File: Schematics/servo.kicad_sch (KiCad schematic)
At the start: 0 parts

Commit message: Power + Servo
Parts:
- added M?: Motor_Servo, symbol Motor:Motor_Servo
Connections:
- new net +5V: M?.2 (+)
- new net Earth: M?.3 (-)
- new net ServoPWM: M?.1 (PWM)
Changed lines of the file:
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@@
 (kicad_sch (version 20211123) (generator eeschema)
   (paper "A4")
+  (wire (pts (xy 137.16 102.87) (xy 137.16 101.6))
+    (stroke (width 0) (type default) (color 0 0 0 0))
+  )
+  (wire (pts (xy 143.51 100.33) (xy 140.97 100.33))
+    (stroke (width 0) (type default) (color 0 0 0 0))
+  )
+  (wire (pts (xy 140.97 100.33) (xy 140.97 95.25))
+    (stroke (width 0) (type default) (color 0 0 0 0))
+  )
+  (wire (pts (xy 143.51 105.41) (xy 137.16 105.41))
+    (stroke (width 0) (type default) (color 0 0 0 0))
+  )
+  (wire (pts (xy 143.51 102.87) (xy 137.16 102.87))
+    (stroke (width 0) (type default) (color 0 0 0 0))
+  )
+  (wire (pts (xy 137.16 105.41) (xy 137.16 106.68))
+    (stroke (width 0) (type default) (color 0 0 0 0))
+  )
+  (wire (pts (xy 140.97 95.25) (xy 146.05 95.25))
+    (stroke (width 0) (type default) (color 0 0 0 0))
+  )
+  (global_label "ServoPWM" (shape input) (at 146.05 95.25 0) (fields_autoplaced)
+    (effects (font (size 1.27 1.27)) (justify left))
+    (property "Intersheet References" "${INTERSHEET_REFS}" (id 0) (at 157.8369 95.1706 0)
+      (effects (font (size 1.27 1.27)) (justify left) hide)
+    )
+  )
+  (symbol (lib_id "power:+5V") (at 137.16 101.6 0) (unit 1)
+    (in_bom yes) (on_board yes) (fields_autoplaced)
+    (property "Reference" "#PWR?" (id 0) (at 137.16 105.41 0)
+      (effects (font (size 1.27 1.27)) hide)
+    )
+    (property "Value" "+5V" (id 1) (at 137.16 96.52 0))
+    (property "Footprint" "" (id 2) (at 137.16 101.6 0)
+      (effects (font (size 1.27 1.27)) hide)
+    )
+    (property "Datasheet" "" (id 3) (at 137.16 101.6 0)
+      (effects (font (size 1.27 1.27)) hide)
+    )
+    (pin "1")
+  )
+  (symbol (lib_id "power:Earth") (at 137.16 106.68 0) (unit 1)
+    (in_bom yes) (on_board yes) (fields_autoplaced)
+    (property "Reference" "#PWR?" (id 0) (at 137.16 113.03 0)
+      (effects (font (size 1.27 1.27)) hide)
+    )
+    (property "Value" "Earth" (id 1) (at 137.16 110.49 0)
+      (effects (font (size 1.27 1.27)) hide)
+    )
+    (property "Footprint" "" (id 2) (at 137.16 106.68 0)
+      (effects (font (size 1.27 1.27)) hide)
+    )
+    (property "Datasheet" "~" (id 3) (at 137.16 106.68 0)
+      (effects (font (size 1.27 1.27)) hide)
+    )
+    (pin "1")
+  )
+  (symbol (lib_id "Motor:Motor_Servo") (at 151.13 102.87 0) (unit 1)
+    (in_bom yes) (on_board yes) (fields_autoplaced)
+    (property "Reference" "M?" (id 0) (at 160.02 101.1665 0)
+      (effects (font (size 1.27 1.27)) (justify left))
+    )
+    (property "Value" "Motor_Servo" (id 1) (at 160.02 103.7065 0)
+      (effects (font (size 1.27 1.27)) (justify left))
+    )
+    (property "Footprint" "" (id 2) (at 151.13 107.696 0)
+      (effects (font (size 1.27 1.27)) hide)
+    )
+    (property "Datasheet" "http://forums.parallax.com/uploads/attachments/46831/74481.png" (id 3) (at 151.13 107.696 0)
+      (effects (font (size 1.27 1.27)) hide)
+    )
+    (pin "1")
+    (pin "2")
+    (pin "3")
+  )
 )

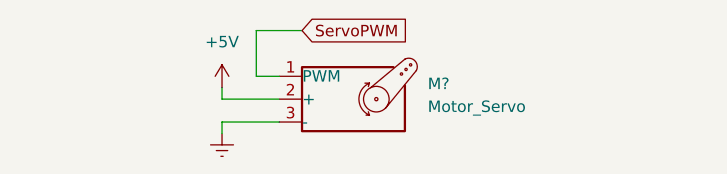
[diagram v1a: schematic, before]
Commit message: Changed MCU
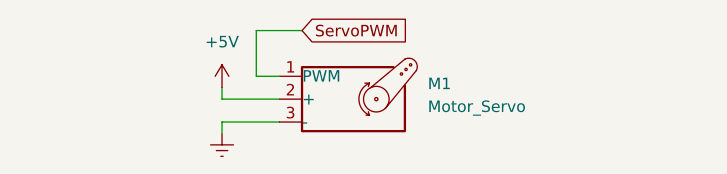
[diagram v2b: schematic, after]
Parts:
- gave numbers to parts that had none: 1
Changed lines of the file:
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@@
   (symbol (lib_id "power:+5V") (at 137.16 101.6 0) (unit 1)
     (in_bom yes) (on_board yes) (fields_autoplaced)
-    (property "Reference" "#PWR?" (id 0) (at 137.16 105.41 0)
+    (property "Reference" "#PWR021" (id 0) (at 137.16 105.41 0)
       (effects (font (size 1.27 1.27)) hide)
     )
@@
   (symbol (lib_id "power:Earth") (at 137.16 106.68 0) (unit 1)
     (in_bom yes) (on_board yes) (fields_autoplaced)
-    (property "Reference" "#PWR?" (id 0) (at 137.16 113.03 0)
+    (property "Reference" "#PWR022" (id 0) (at 137.16 113.03 0)
       (effects (font (size 1.27 1.27)) hide)
     )
@@
   (symbol (lib_id "Motor:Motor_Servo") (at 151.13 102.87 0) (unit 1)
     (in_bom yes) (on_board yes) (fields_autoplaced)
-    (property "Reference" "M?" (id 0) (at 160.02 101.1665 0)
+    (property "Reference" "M1" (id 0) (at 160.02 101.1665 0)
       (effects (font (size 1.27 1.27)) (justify left))
     )

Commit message: Added Footprints
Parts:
- M1: footprint (none) -> SFRFootprints:Servo
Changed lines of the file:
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@@
       (effects (font (size 1.27 1.27)) (justify left))
     )
-    (property "Footprint" "" (id 2) (at 151.13 107.696 0)
+    (property "Footprint" "SFRFootprints:Servo" (id 2) (at 151.13 107.696 0)
       (effects (font (size 1.27 1.27)) hide)
     )

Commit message: PCB
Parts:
- added M2: Motor_Servo, SFRFootprints:Servo, symbol Motor:Motor_Servo
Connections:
- net +5V: now also M2.2 (+)
- net Earth: now also M2.3 (-)
- net ServoPWM renamed ServoPWM1
- new net ServoPWM2: M2.1 (PWM)
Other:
- moved on the sheet: M1
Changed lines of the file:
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@@
 (kicad_sch (version 20211123) (generator eeschema)
   (paper "A4")
-  (wire (pts (xy 137.16 102.87) (xy 137.16 101.6))
+  (wire (pts (xy 116.84 102.87) (xy 116.84 101.6))
     (stroke (width 0) (type default) (color 0 0 0 0))
   )
-  (wire (pts (xy 143.51 100.33) (xy 140.97 100.33))
+  (wire (pts (xy 160.655 100.33) (xy 158.115 100.33))
     (stroke (width 0) (type default) (color 0 0 0 0))
   )
-  (wire (pts (xy 140.97 100.33) (xy 140.97 95.25))
+  (wire (pts (xy 158.115 95.25) (xy 163.195 95.25))
     (stroke (width 0) (type default) (color 0 0 0 0))
   )
-  (wire (pts (xy 143.51 105.41) (xy 137.16 105.41))
+  (wire (pts (xy 158.115 100.33) (xy 158.115 95.25))
     (stroke (width 0) (type default) (color 0 0 0 0))
   )
-  (wire (pts (xy 143.51 102.87) (xy 137.16 102.87))
+  (wire (pts (xy 123.19 100.33) (xy 120.65 100.33))
     (stroke (width 0) (type default) (color 0 0 0 0))
   )
-  (wire (pts (xy 137.16 105.41) (xy 137.16 106.68))
+  (wire (pts (xy 154.305 105.41) (xy 154.305 106.68))
     (stroke (width 0) (type default) (color 0 0 0 0))
   )
-  (wire (pts (xy 140.97 95.25) (xy 146.05 95.25))
+  (wire (pts (xy 120.65 100.33) (xy 120.65 95.25))
     (stroke (width 0) (type default) (color 0 0 0 0))
   )
-  (global_label "ServoPWM" (shape input) (at 146.05 95.25 0) (fields_autoplaced)
+  (wire (pts (xy 123.19 105.41) (xy 116.84 105.41))
+    (stroke (width 0) (type default) (color 0 0 0 0))
+  )
+  (wire (pts (xy 154.305 102.87) (xy 154.305 101.6))
+    (stroke (width 0) (type default) (color 0 0 0 0))
+  )
+  (wire (pts (xy 160.655 105.41) (xy 154.305 105.41))
+    (stroke (width 0) (type default) (color 0 0 0 0))
+  )
+  (wire (pts (xy 160.655 102.87) (xy 154.305 102.87))
+    (stroke (width 0) (type default) (color 0 0 0 0))
+  )
+  (wire (pts (xy 123.19 102.87) (xy 116.84 102.87))
+    (stroke (width 0) (type default) (color 0 0 0 0))
+  )
+  (wire (pts (xy 116.84 105.41) (xy 116.84 106.68))
+    (stroke (width 0) (type default) (color 0 0 0 0))
+  )
+  (wire (pts (xy 120.65 95.25) (xy 125.73 95.25))
+    (stroke (width 0) (type default) (color 0 0 0 0))
+  )
+  (global_label "ServoPWM1" (shape input) (at 125.73 95.25 0) (fields_autoplaced)
     (effects (font (size 1.27 1.27)) (justify left))
-    (property "Intersheet References" "${INTERSHEET_REFS}" (id 0) (at 157.8369 95.1706 0)
+    (property "Intersheet References" "${INTERSHEET_REFS}" (id 0) (at 138.7264 95.1706 0)
       (effects (font (size 1.27 1.27)) (justify left) hide)
     )
   )
-  (symbol (lib_id "power:+5V") (at 137.16 101.6 0) (unit 1)
+  (global_label "ServoPWM2" (shape input) (at 163.195 95.25 0) (fields_autoplaced)
+    (effects (font (size 1.27 1.27)) (justify left))
+    (property "Intersheet References" "${INTERSHEET_REFS}" (id 0) (at 176.1914 95.1706 0)
+      (effects (font (size 1.27 1.27)) (justify left) hide)
+    )
+  )
+  (symbol (lib_id "power:Earth") (at 154.305 106.68 0) (unit 1)
     (in_bom yes) (on_board yes) (fields_autoplaced)
-    (property "Reference" "#PWR021" (id 0) (at 137.16 105.41 0)
+    (property "Reference" "#PWR0102" (id 0) (at 154.305 113.03 0)
       (effects (font (size 1.27 1.27)) hide)
     )
-    (property "Value" "+5V" (id 1) (at 137.16 96.52 0))
-    (property "Footprint" "" (id 2) (at 137.16 101.6 0)
+    (property "Value" "Earth" (id 1) (at 154.305 110.49 0)
       (effects (font (size 1.27 1.27)) hide)
     )
-    (property "Datasheet" "" (id 3) (at 137.16 101.6 0)
+    (property "Footprint" "" (id 2) (at 154.305 106.68 0)
+      (effects (font (size 1.27 1.27)) hide)
+    )
+    (property "Datasheet" "~" (id 3) (at 154.305 106.68 0)
       (effects (font (size 1.27 1.27)) hide)
     )
     (pin "1")
   )
-  (symbol (lib_id "power:Earth") (at 137.16 106.68 0) (unit 1)
+  (symbol (lib_id "power:+5V") (at 116.84 101.6 0) (unit 1)
     (in_bom yes) (on_board yes) (fields_autoplaced)
-    (property "Reference" "#PWR022" (id 0) (at 137.16 113.03 0)
+    (property "Reference" "#PWR021" (id 0) (at 116.84 105.41 0)
       (effects (font (size 1.27 1.27)) hide)
     )
-    (property "Value" "Earth" (id 1) (at 137.16 110.49 0)
+    (property "Value" "+5V" (id 1) (at 116.84 96.52 0))
+    (property "Footprint" "" (id 2) (at 116.84 101.6 0)
       (effects (font (size 1.27 1.27)) hide)
     )
-    (property "Footprint" "" (id 2) (at 137.16 106.68 0)
-      (effects (font (size 1.27 1.27)) hide)
-    )
-    (property "Datasheet" "~" (id 3) (at 137.16 106.68 0)
+    (property "Datasheet" "" (id 3) (at 116.84 101.6 0)
       (effects (font (size 1.27 1.27)) hide)
     )
     (pin "1")
   )
-  (symbol (lib_id "Motor:Motor_Servo") (at 151.13 102.87 0) (unit 1)
+  (symbol (lib_id "Motor:Motor_Servo") (at 168.275 102.87 0) (unit 1)
     (in_bom yes) (on_board yes) (fields_autoplaced)
-    (property "Reference" "M1" (id 0) (at 160.02 101.1665 0)
+    (property "Reference" "M2" (id 0) (at 177.165 101.1665 0)
       (effects (font (size 1.27 1.27)) (justify left))
     )
-    (property "Value" "Motor_Servo" (id 1) (at 160.02 103.7065 0)
+    (property "Value" "Motor_Servo" (id 1) (at 177.165 103.7065 0)
       (effects (font (size 1.27 1.27)) (justify left))
     )
-    (property "Footprint" "SFRFootprints:Servo" (id 2) (at 151.13 107.696 0)
+    (property "Footprint" "SFRFootprints:Servo" (id 2) (at 168.275 107.696 0)
       (effects (font (size 1.27 1.27)) hide)
     )
-    (property "Datasheet" "http://forums.parallax.com/uploads/attachments/46831/74481.png" (id 3) (at 151.13 107.696 0)
+    (property "Datasheet" "http://forums.parallax.com/uploads/attachments/46831/74481.png" (id 3) (at 168.275 107.696 0)
       (effects (font (size 1.27 1.27)) hide)
     )
+    (pin "1")
+    (pin "2")
+    (pin "3")
+  )
+  (symbol (lib_id "power:Earth") (at 116.84 106.68 0) (unit 1)
+    (in_bom yes) (on_board yes) (fields_autoplaced)
+    (property "Reference" "#PWR022" (id 0) (at 116.84 113.03 0)
+      (effects (font (size 1.27 1.27)) hide)
+    )
+    (property "Value" "Earth" (id 1) (at 116.84 110.49 0)
+      (effects (font (size 1.27 1.27)) hide)
+    )
+    (property "Footprint" "" (id 2) (at 116.84 106.68 0)
+      (effects (font (size 1.27 1.27)) hide)
+    )
+    (property "Datasheet" "~" (id 3) (at 116.84 106.68 0)
+      (effects (font (size 1.27 1.27)) hide)
+    )
+    (pin "1")
+  )
+  (symbol (lib_id "power:+5V") (at 154.305 101.6 0) (unit 1)
+    (in_bom yes) (on_board yes) (fields_autoplaced)
+    (property "Reference" "#PWR0103" (id 0) (at 154.305 105.41 0)
+      (effects (font (size 1.27 1.27)) hide)
+    )
+    (property "Value" "+5V" (id 1) (at 154.305 96.52 0))
+    (property "Footprint" "" (id 2) (at 154.305 101.6 0)
+      (effects (font (size 1.27 1.27)) hide)
+    )
+    (property "Datasheet" "" (id 3) (at 154.305 101.6 0)
+      (effects (font (size 1.27 1.27)) hide)
+    )
+    (pin "1")
+  )
+  (symbol (lib_id "Motor:Motor_Servo") (at 130.81 102.87 0) (unit 1)
+    (in_bom yes) (on_board yes) (fields_autoplaced)
+    (property "Reference" "M1" (id 0) (at 139.7 101.1665 0)
+      (effects (font (size 1.27 1.27)) (justify left))
+    )
+    (property "Value" "Motor_Servo" (id 1) (at 139.7 103.7065 0)
+      (effects (font (size 1.27 1.27)) (justify left))
+    )
+    (property "Footprint" "SFRFootprints:Servo" (id 2) (at 130.81 107.696 0)
+      (effects (font (size 1.27 1.27)) hide)
+    )
+    (property "Datasheet" "http://forums.parallax.com/uploads/attachments/46831/74481.png" (id 3) (at 130.81 107.696 0)
+      (effects (font (size 1.27 1.27)) hide)
+    )
